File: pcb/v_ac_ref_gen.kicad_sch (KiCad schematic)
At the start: 30 parts

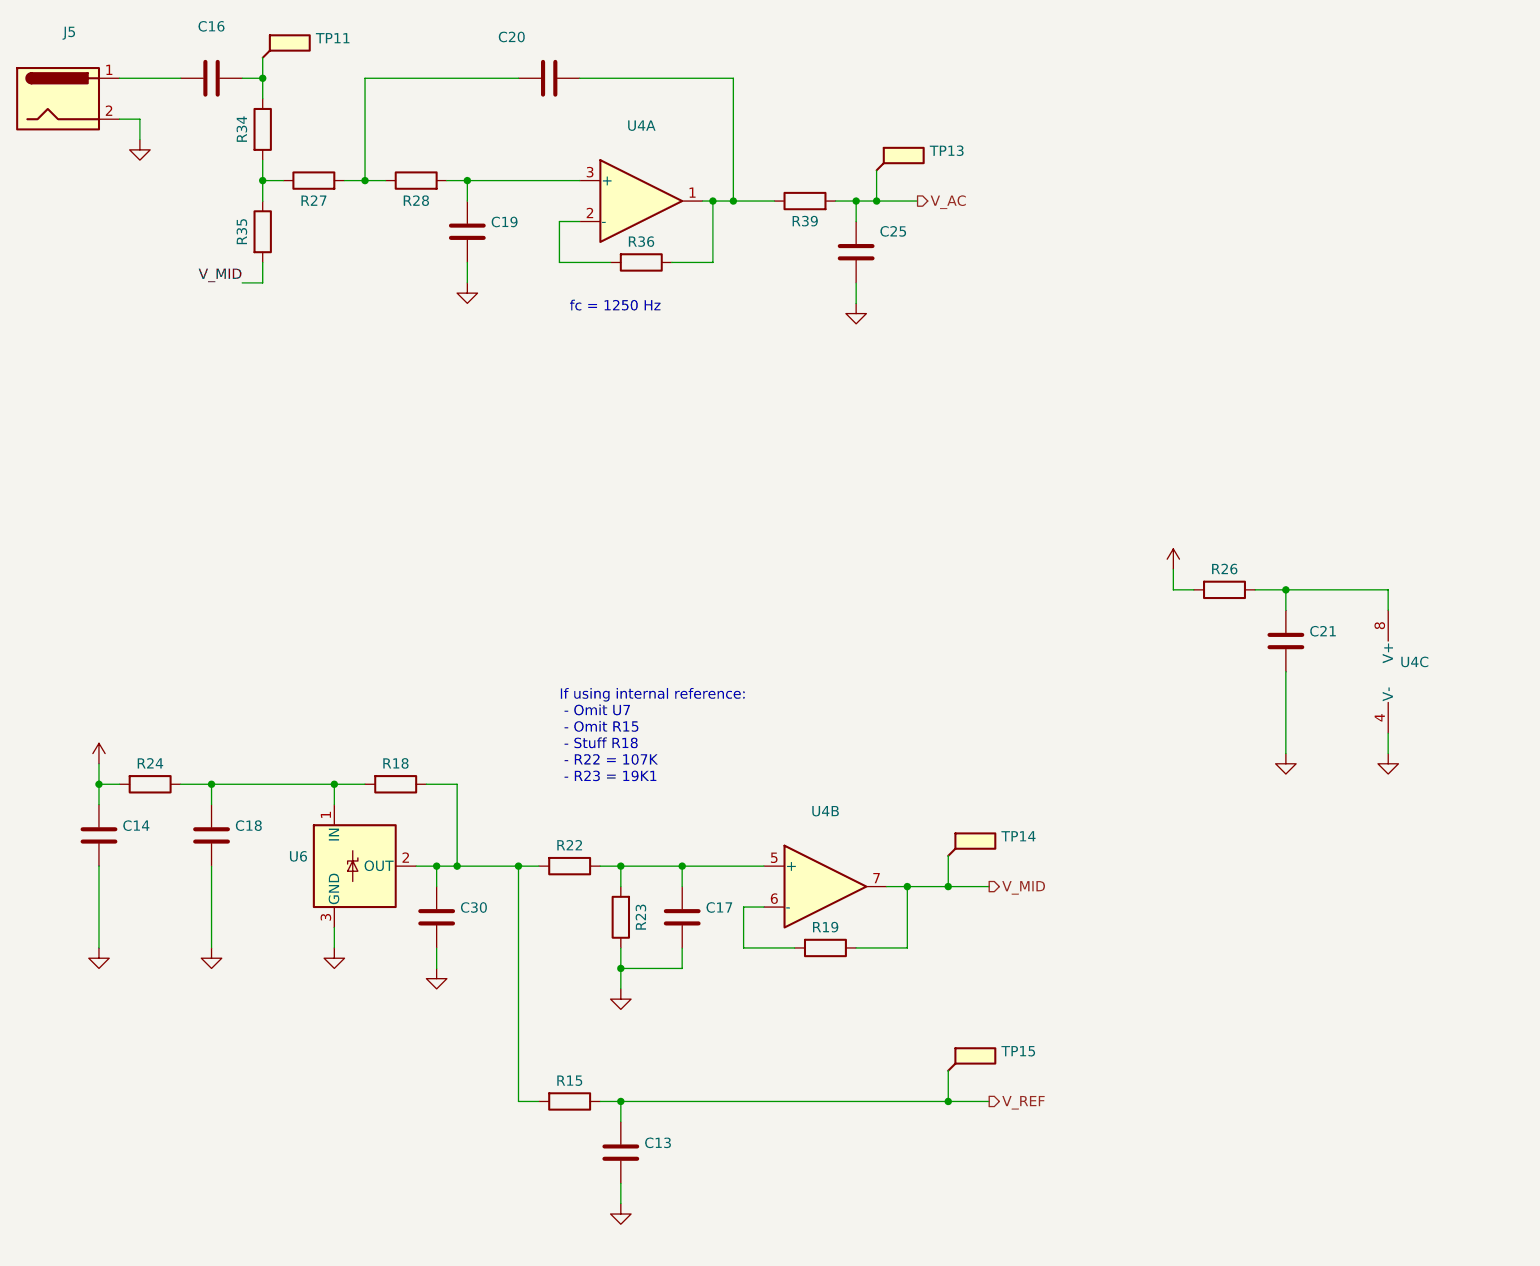
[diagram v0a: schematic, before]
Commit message: * Start replicating emonLibCM functionality
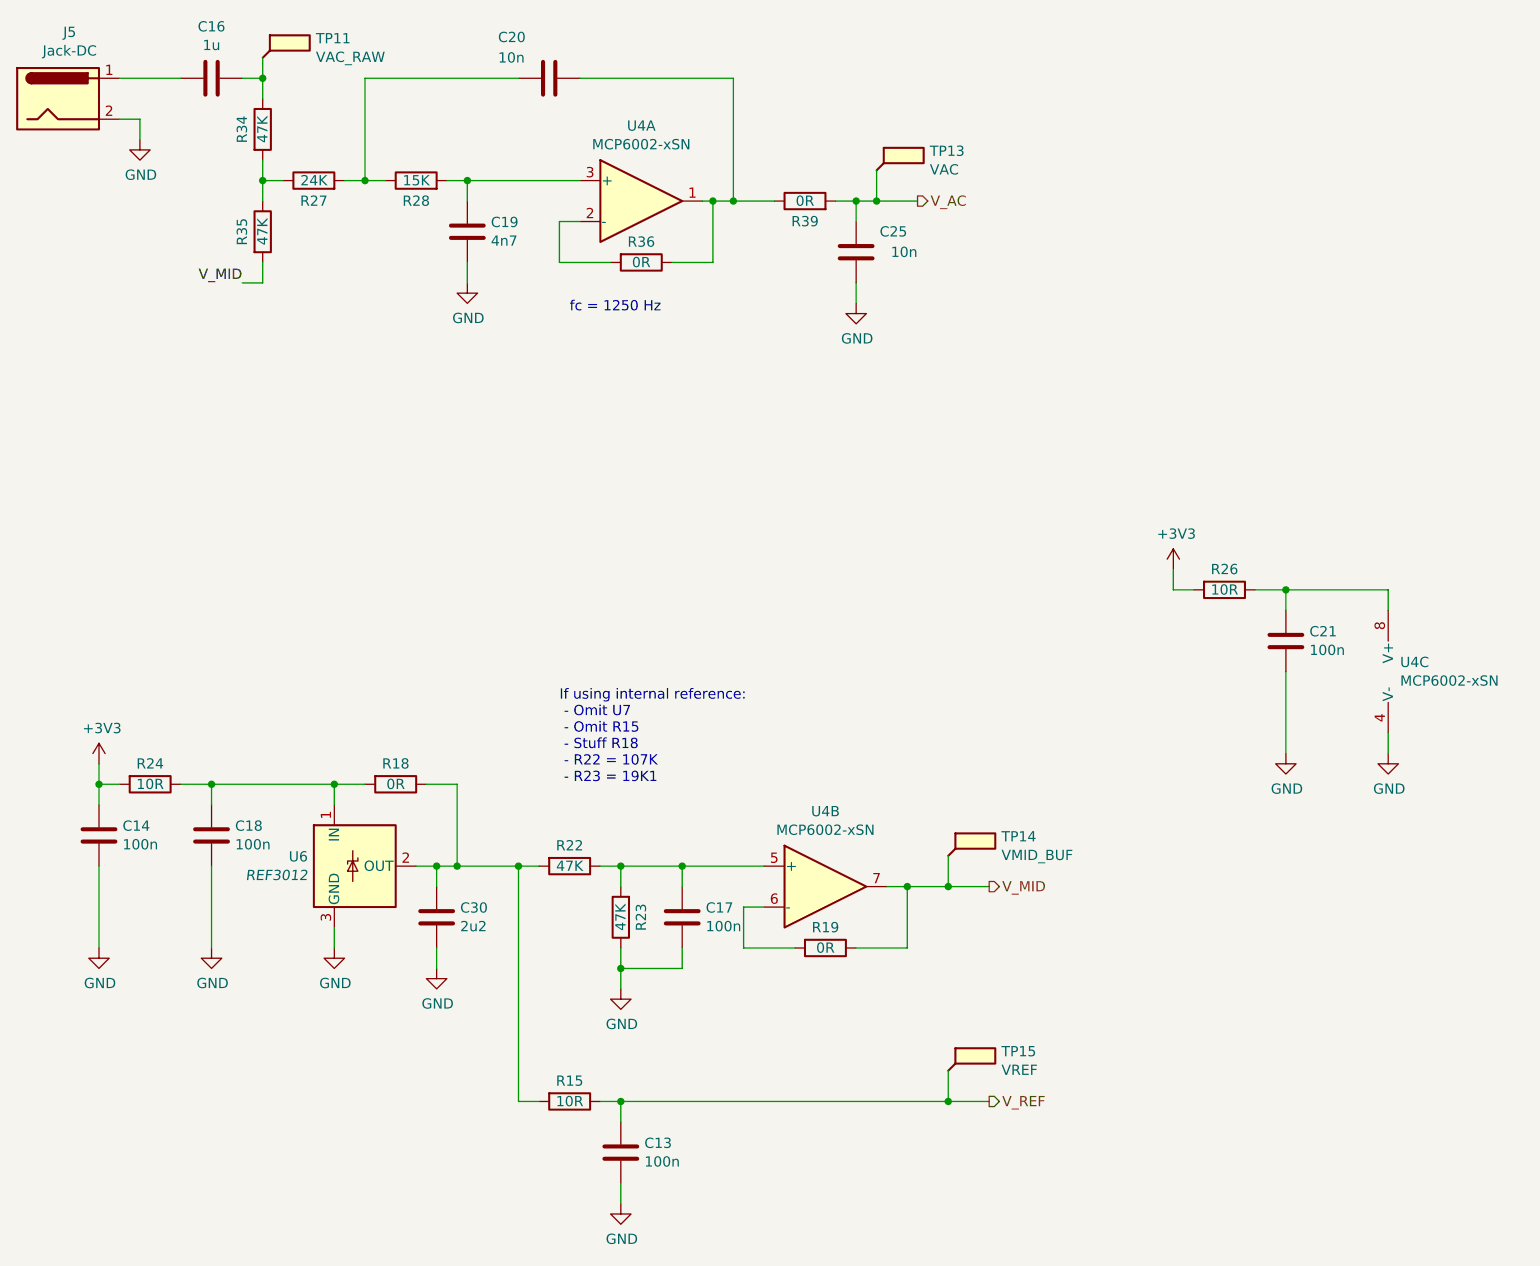
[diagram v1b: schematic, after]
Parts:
- C13, C14, C17, C18, C21: value (none) -> 100n; footprint (none) -> Capacitor_SMD:C_0805_2012Metric_Pad1.18x1.45mm_HandSolder
- C16: value (none) -> 1u; footprint (none) -> Capacitor_SMD:C_0805_2012Metric_Pad1.18x1.45mm_HandSolder
- C19: value (none) -> 4n7; footprint (none) -> Capacitor_SMD:C_0805_2012Metric_Pad1.18x1.45mm_HandSolder
- C20, C25: value (none) -> 10n; footprint (none) -> Capacitor_SMD:C_0805_2012Metric_Pad1.18x1.45mm_HandSolder
- C30: value (none) -> 2u2; footprint (none) -> Capacitor_SMD:C_0805_2012Metric_Pad1.18x1.45mm_HandSolder
- J5: value (none) -> Jack-DC; footprint (none) -> Connector_BarrelJack:BarrelJack_CUI_PJ-063AH_Horizontal
- R15, R24, R26: value (none) -> 10R; footprint (none) -> Resistor_SMD:R_0805_2012Metric_Pad1.20x1.40mm_HandSolder
- R18, R19, R36, R39: value (none) -> 0R; footprint (none) -> Resistor_SMD:R_0805_2012Metric_Pad1.20x1.40mm_HandSolder
- R22, R23, R34, R35: value (none) -> 47K; footprint (none) -> Resistor_SMD:R_0805_2012Metric_Pad1.20x1.40mm_HandSolder
- R27: value (none) -> 24K; footprint (none) -> Resistor_SMD:R_0805_2012Metric_Pad1.20x1.40mm_HandSolder
- R28: value (none) -> 15K; footprint (none) -> Resistor_SMD:R_0805_2012Metric_Pad1.20x1.40mm_HandSolder
- TP11: value (none) -> VAC_RAW; footprint (none) -> TestPoint:TestPoint_THTPad_1.5x1.5mm_Drill0.7mm
- TP13: value (none) -> VAC; footprint (none) -> TestPoint:TestPoint_THTPad_1.5x1.5mm_Drill0.7mm
- TP14: value (none) -> VMID_BUF; footprint (none) -> TestPoint:TestPoint_THTPad_1.5x1.5mm_Drill0.7mm
- TP15: value (none) -> VREF; footprint (none) -> TestPoint:TestPoint_THTPad_1.5x1.5mm_Drill0.7mm
- U4: value (none) -> MCP6002-xSN; footprint (none) -> Package_SO:SOIC-8_3.9x4.9mm_P1.27mm
- U6: value (none) -> REF3012; footprint (none) -> Package_TO_SOT_SMD:SOT-23
